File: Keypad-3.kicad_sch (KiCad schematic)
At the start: 20 parts, among them SW1 SW_Push, U1 ATmega32U4-A, Y1 16MHz

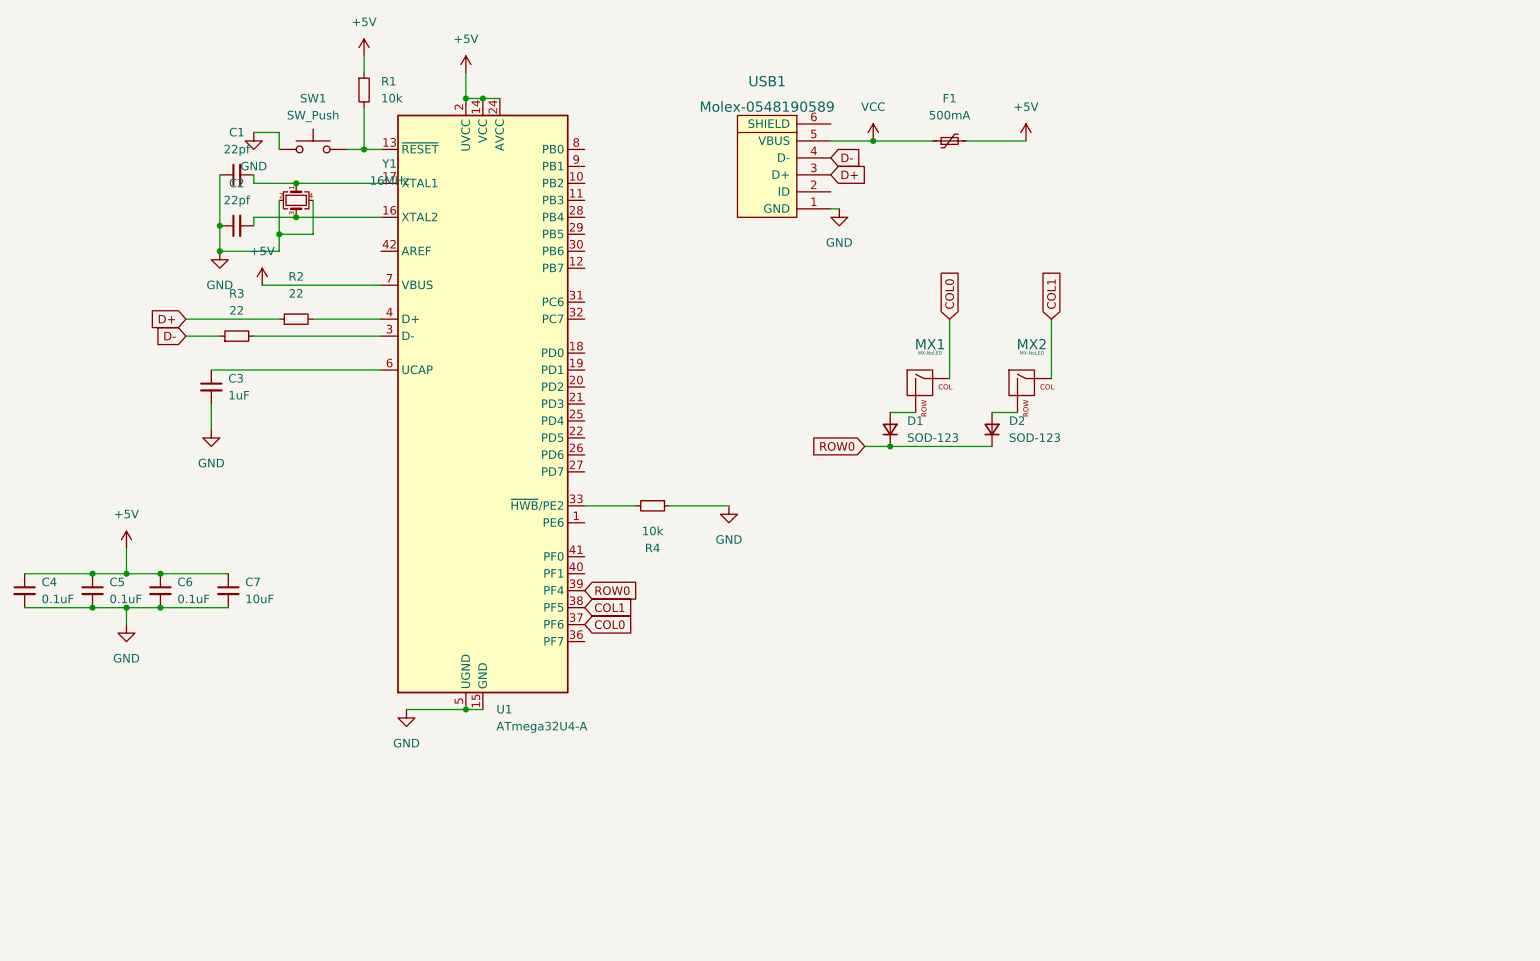
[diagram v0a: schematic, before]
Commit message: Fixed usb c tracing
I made the usb-c traces straight and re arranged the board to a different layout
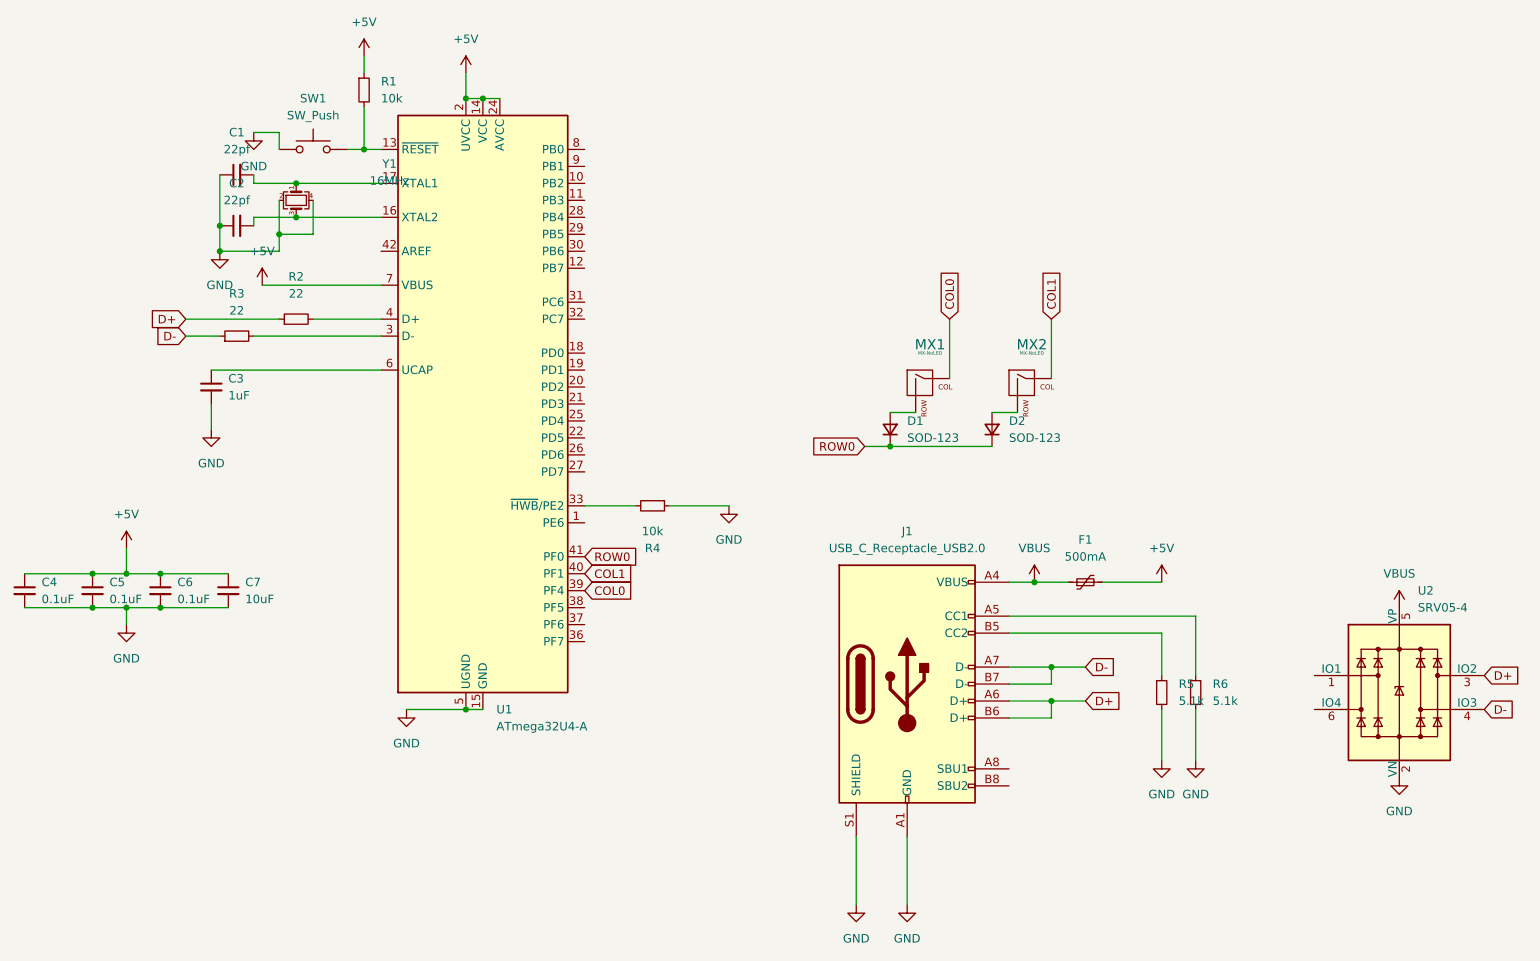
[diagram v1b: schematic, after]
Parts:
- removed USB1: Molex-0548190589, random-keyboard-parts:Molex-0548190589, symbol random-keyboard-parts:Molex-0548190589
- added J1: USB_C_Receptacle_USB2.0, Connector_USB:USB_C_Receptacle_HRO_TYPE-C-31-M-12, symbol Connector:USB_C_Receptacle_USB2.0
- added R5, R6: 5.1k, Resistor_SMD:R_0805_2012Metric, symbol Device:R_Small
- added U2: SRV05-4, marbastlib-various:SOT-23-6-routable, symbol marbastlib-various:SRV05-4
- C1: footprint Capacitor_SMD:C_0805_2012Metric -> Resistor_SMD:R_0805_2012Metric
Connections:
- net COL0: now also U1.39 (PF4); no longer U1.37 (PF6)
- net COL1: now also U1.40 (PF1); no longer U1.38 (PF5)
- net D+: now also J1.A6 (D+), J1.B6 (D+), U2.3 (IO2)
- net D-: now also J1.A7 (D-), J1.B7 (D-), U2.4 (IO3)
- net GND: now also J1.A1 (GND), J1.A12 (GND), J1.B1 (GND), J1.B12 (GND), J1.S1 (SHIELD), R5.2, R6.2, U2.2 (VN)
- net ROW0: now also U1.41 (PF0); no longer U1.39 (PF4)
- net VCC renamed VBUS
- net VBUS: now also J1.A4 (VBUS), J1.A9 (VBUS), J1.B4 (VBUS), J1.B9 (VBUS), U2.5 (VP)
- new net: J1.B5 (CC2), R5.1
- new net: J1.A5 (CC1), R6.1
